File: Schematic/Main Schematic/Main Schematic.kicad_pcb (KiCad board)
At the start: 2 copper layers, 100 x 100 mm, 49 parts, among them IC1 DW01A-G, IC2 LM75AD,118, J1 Conn_01x24_Socket, J10 Conn_01x08_Pin, J2 Conn_01x02_Pin, J3 Conn_01x24_Socket, J4 Conn_01x02_Male, J5 Conn_01x02_Male, J6 USB_B_Micro, J7 Conn_01x02_Pin, J8 Conn_01x24_Pin, J9 Conn_01x24_Pin, Q1 FS8205A, SW1 SW_Push, U1 HT75xx-1-SOT89, U2 MCP73831-2-OT, U3 CH340C, U4 M24C16-RMN6TP

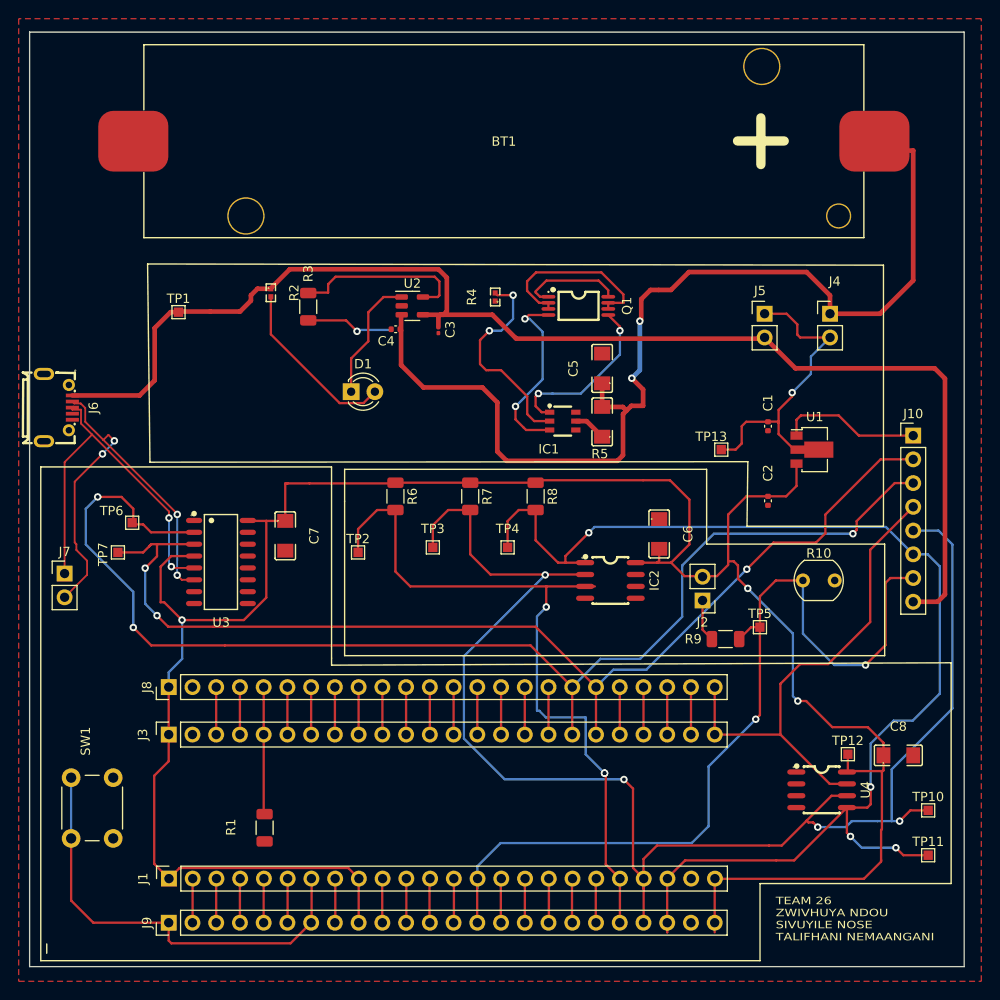
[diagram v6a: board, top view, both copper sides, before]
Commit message: Added more led for visual indications, also changed debugger pins to 9 pins for 3.3v pin
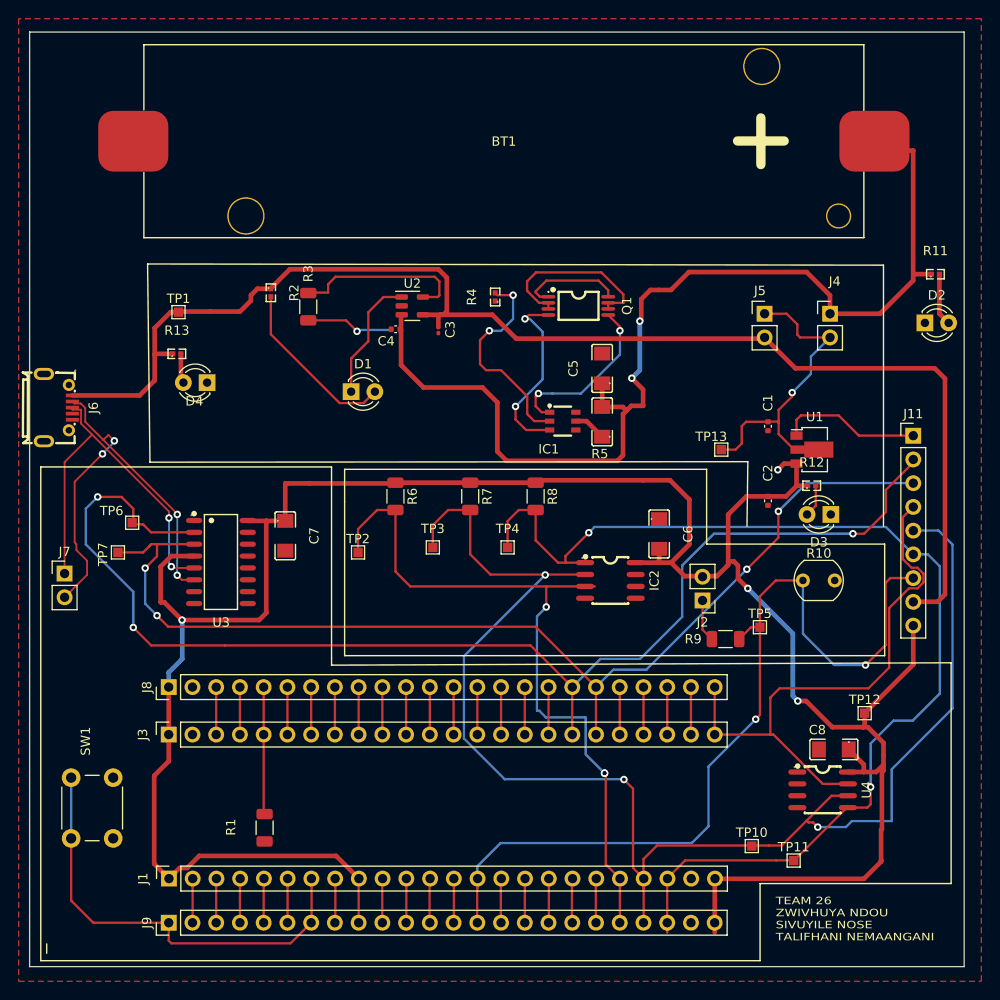
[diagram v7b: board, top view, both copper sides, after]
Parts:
- removed J10: Conn_01x08_Pin, Connector_PinHeader_2.54mm:PinHeader_1x08_P2.54mm_Vertical
- added D2: LED, LED_THT:LED_D3.0mm, F.Cu at (197.0, 69.5)
- added D3: LED, LED_THT:LED_D3.0mm, F.Cu at (186.9, 90.0)
- added D4: LED, LED_THT:LED_D3.0mm, F.Cu at (120.2, 75.9)
- added J11: Conn_01x09_Pin, Connector_PinHeader_2.54mm:PinHeader_1x09_P2.54mm_Vertical, F.Cu at (195.7, 81.6)
- added R11: 1k, Local_Footprints:R0402, F.Cu at (198.1, 64.3)
- added R12: 1k, Local_Footprints:R0402, F.Cu at (184.9, 87.0)
- added R13: 1k, Local_Footprints:R0402, F.Cu at (116.9, 72.9)
- moved TP10 19.3 mm to (178.4, 125.5)
- moved TP11 14.4 mm to (182.9, 127.1)
- moved C8 6.93 mm to (187.2, 115.2), turned to 180 degrees
- moved TP12 4.74 mm to (190.5, 111.3)
- moved U4 0.11 mm to (186.0, 119.5)
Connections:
- J2 pad 1: (no net) -> Net-(J2-Pin_1)
- J3 pad 19: (no net) -> /TXD
- J8 pad 19: (no net) -> /TXD
- R9 pad 1: (no net) -> Net-(J2-Pin_1)
- TP6 pad 1: /RXD -> /TXD
- TP7 pad 1: (no net) -> /RXD
- U3 pad 3: (no net) -> /TXD
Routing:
- net /3.3V: track 245.9 -> 265.9 mm, vias 3 -> 4
- net /SDL: track 132.6 -> 120.2 mm, vias 4 -> 2
- net /WRITE: track 53.4 -> 60.5 mm
- net Net-(D2-A): track 0.00 -> 5.62 mm
- net /SCL: track 160.7 -> 156.3 mm, vias 4 -> 3
- net Net-(D3-A): track 0.00 -> 3.47 mm
- net Net-(D4-A): track 0.00 -> 3.19 mm
- net /RXD: track 133.5 -> 135.5 mm
- net /5V: track 141.2 -> 143.1 mm
- net /Power Unit/V1: track 114.9 -> 116.8 mm
- net /TXD: track 122.2 -> 121.7 mm, vias 3 -> 4

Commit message: Edit
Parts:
- moved TP7 3.31 mm to (113.5, 95.8), turned to 0 degrees
- moved TP6 1.57 mm to (113.3, 92.0)
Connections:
- TP6 pad 1: /TXD -> /RXD
- TP7 pad 1: /RXD -> /TXD
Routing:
- net /RXD: track 135.5 -> 124.5 mm, vias 3 -> 1
- net GND: track 43.7 -> 34.6 mm, vias 1 -> 0
- net /WRITE: track 60.5 -> 52.1 mm
- net /TXD: track 121.7 -> 113.4 mm, vias 4 -> 2
- net Net-(J2-Pin_1): track 0.00 -> 4.54 mm
- net /Power Unit/V1: track 116.8 -> 115.1 mm
- net Net-(D1-A): track 18.7 -> 19.3 mm
